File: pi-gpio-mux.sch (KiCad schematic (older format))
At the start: 31 parts, among them J1 Raspberry_Pi_2_3, J2 Raw, J3 Buffered, J4 Register-1, J5 Register-2, J6 Clk1, J7 Clk1, U1 74AHCT245, U10 74AHCT574, U11 74AHCT574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

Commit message: First layout template vias.
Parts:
- J7: value Clk1 -> Clk2
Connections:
- net CLK1: now reaches J6.1 (Pin_1), U5.11 (Cp), U6.11 (Cp), U7.11 (Cp), U8.11 (Cp)
- net CLK2: now reaches J7.1 (Pin_1), U10.11 (Cp), U11.11 (Cp), U12.11 (Cp), U9.11 (Cp)
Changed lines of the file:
@@
 P 9000 3900
 F 0 "J7" V 8964 3812 50  0000 R CNN
-F 1 "Clk1" V 8873 3812 50  0000 R CNN
+F 1 "Clk2" V 8873 3812 50  0000 R CNN
 F 2 "Connector_Pin:Pin_D0.7mm_L6.5mm_W1.8mm_FlatFork" H 9000 3900 50  0001 C CNN
 F 3 "~" H 9000 3900 50  0001 C CNN
@@
 	1    0    0    -1
 $EndComp
+Text Label 4850 4250 0    50   ~ 0
+CLK1
+Text Label 8900 4300 0    50   ~ 0
+CLK2
 $EndSCHEMATC

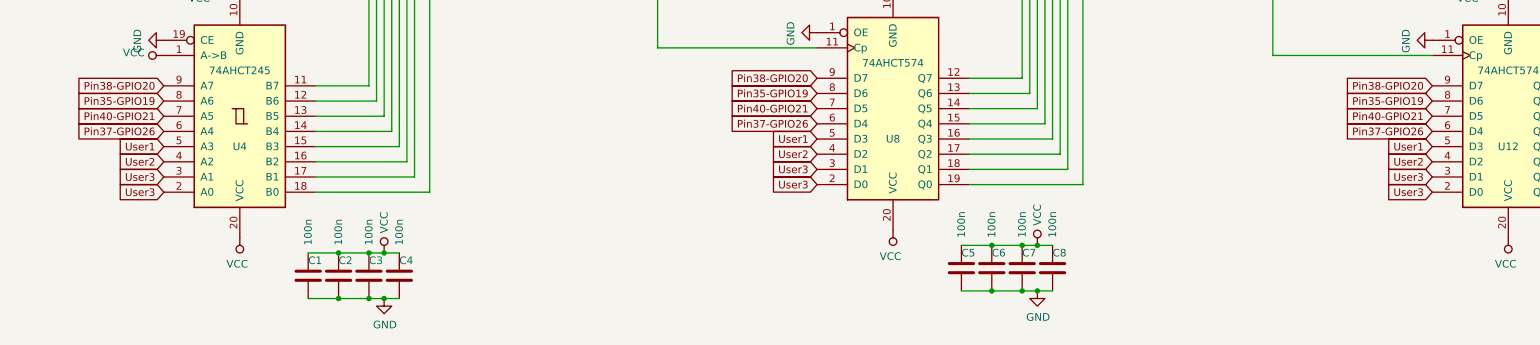
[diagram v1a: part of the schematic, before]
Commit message: trace signal between connectors.
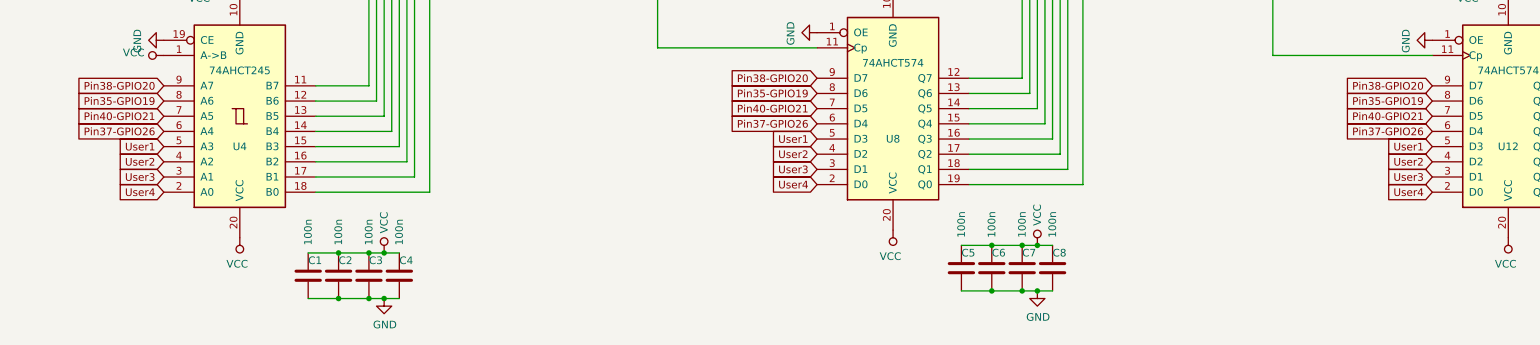
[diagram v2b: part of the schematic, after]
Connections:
- net User3: no longer U12.2 (D0), U4.2 (A0), U8.2 (D0)
- new net User4: U12.2 (D0), U4.2 (A0), U8.2 (D0)
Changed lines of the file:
@@
 User3
 Text GLabel 1600 10200 0    50   Input ~ 0
-User3
+User4
 $Comp
 L 74xx:74HCT574 U5
@@
 User3
 Text GLabel 5900 10150 0    50   Input ~ 0
-User3
+User4
 $Comp
 L 74xx:74HCT574 U6
@@
 User3
 Text GLabel 9950 10200 0    50   Input ~ 0
-User3
+User4
 $Comp
 L 74xx:74HCT574 U10

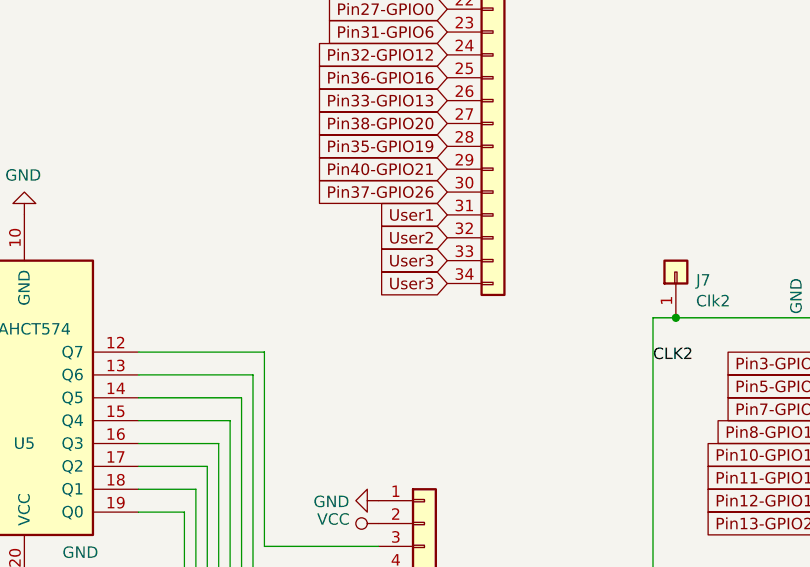
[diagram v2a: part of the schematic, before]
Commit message: Bus connect between registers.
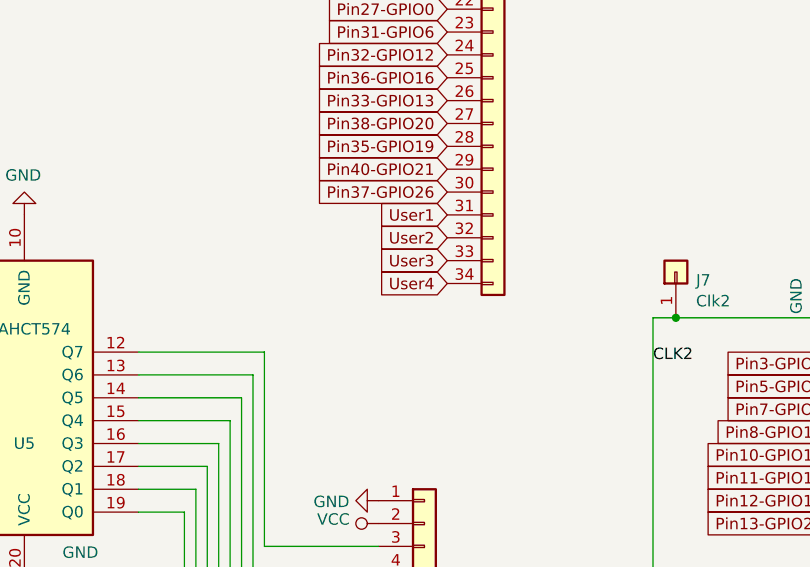
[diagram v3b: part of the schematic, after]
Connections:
- net User3: no longer J2.34 (Pin_34)
- net User4: now also J2.34 (Pin_34)
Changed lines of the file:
@@
 User3
 Text GLabel 8000 3950 0    50   Input ~ 0
-User3
+User4
 Text GLabel 1350 4300 0    50   Input ~ 0
 Pin3-GPIO2

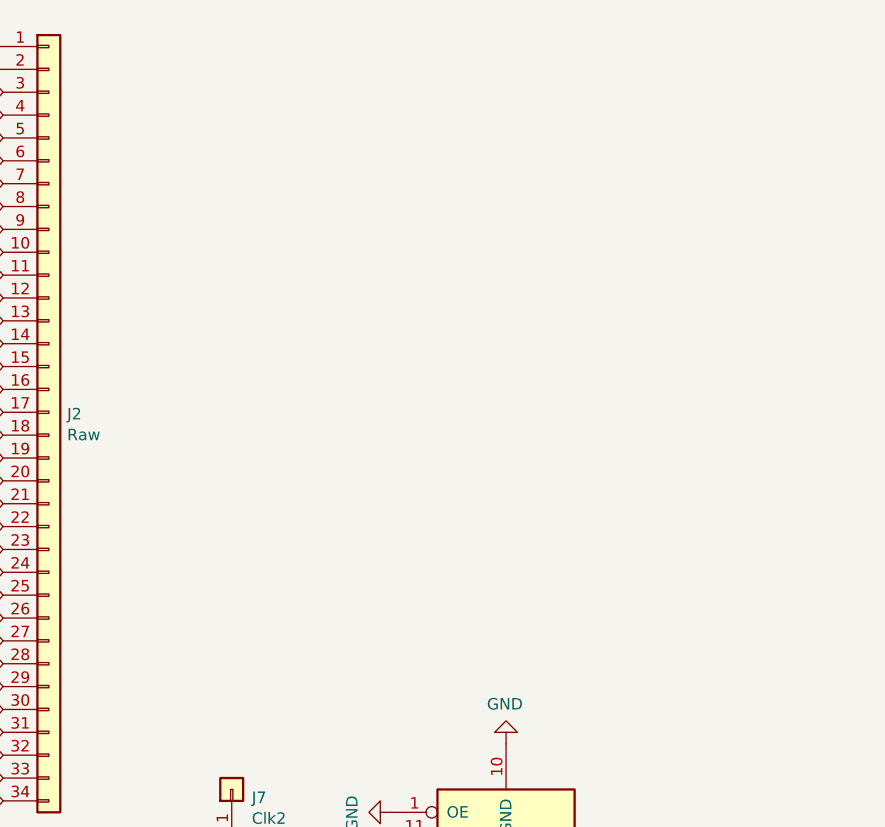
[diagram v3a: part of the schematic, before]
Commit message: Add inverters.
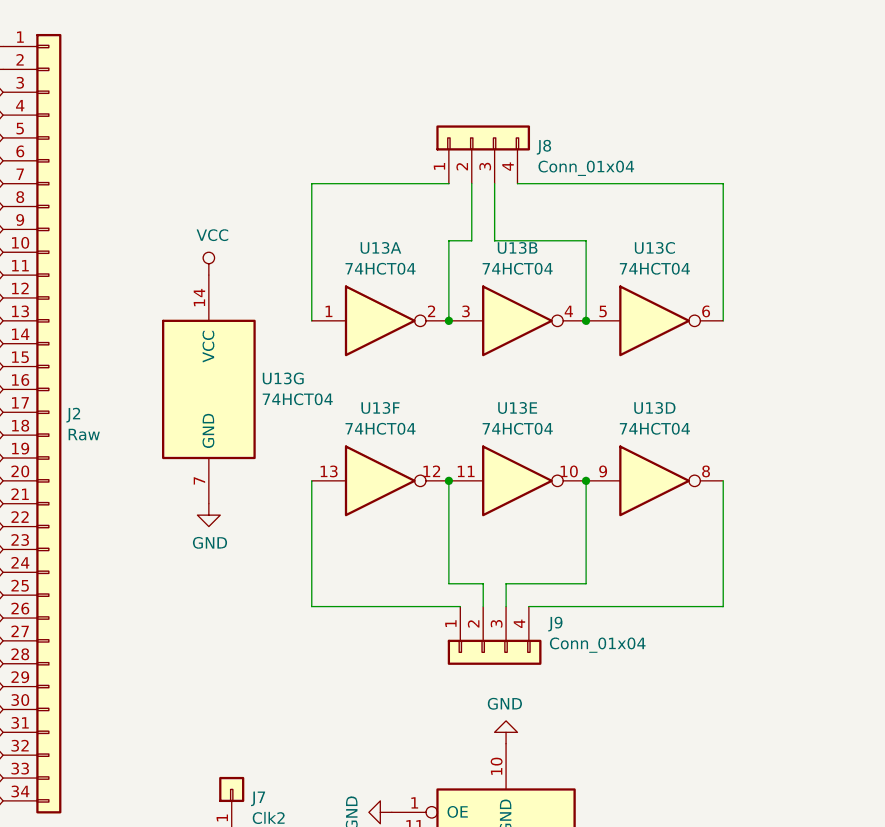
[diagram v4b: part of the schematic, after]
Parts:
- added J8, J9: Conn_01x04, pi-gpio-mux:triple-inverter, symbol Connector_Generic:Conn_01x04
- added U13: 74HCT04, pi-gpio-mux:SOT762-1-DHVQFN14, symbol 74xx:74HCT04
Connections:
- net GND: now also U13.7 (GND)
- net VCC: now also U13.14 (VCC)
- new net: J8.1 (Pin_1), U13.1
- new net: J8.2 (Pin_2), U13.2, U13.3
- new net: J8.3 (Pin_3), U13.4, U13.5
- new net: J8.4 (Pin_4), U13.6
- new net: J9.4 (Pin_4), U13.8
- new net: J9.3 (Pin_3), U13.10, U13.9
- new net: J9.2 (Pin_2), U13.11, U13.12
- new net: J9.1 (Pin_1), U13.13
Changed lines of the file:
@@
 Text Label 8900 4300 0    50   ~ 0
 CLK2
+$Comp
+L power:GND #PWR02
+U 1 1 5D3F4AF0
+P 8900 2650
+F 0 "#PWR02" H 8900 2400 50  0001 C CNN
+F 1 "GND" H 8905 2477 50  0000 C CNN
+F 2 "" H 8900 2650 50  0001 C CNN
+F 3 "" H 8900 2650 50  0001 C CNN
+	1    8900 2650
+	1    0    0    -1
+$EndComp
+$Comp
+L power:VCC #PWR01
+U 1 1 5D3F56BE
+P 8900 1650
+F 0 "#PWR01" H 8900 1500 50  0001 C CNN
+F 1 "VCC" H 8917 1823 50  0000 C CNN
+F 2 "" H 8900 1650 50  0001 C CNN
+F 3 "" H 8900 1650 50  0001 C CNN
+	1    8900 1650
+	1    0    0    -1
+$EndComp
+Wire Wire Line
+	10550 1500 10550 1850
+Wire Wire Line
+	9950 1500 9950 1850
+$Comp
+L 74xx:74HCT04 U13
+U 1 1 5D4B4710
+P 9650 1850
+F 0 "U13" H 9650 2167 50  0000 C CNN
+F 1 "74HCT04" H 9650 2076 50  0000 C CNN
+F 2 "pi-gpio-mux:SOT762-1-DHVQFN14" H 9650 1850 50  0001 C CNN
+F 3 "https://assets.nexperia.com/documents/data-sheet/74HC_HCT04.pdf" H 9650 1850 50  0001 C CNN
+	1    9650 1850
+	1    0    0    -1
+$EndComp
+$Comp
+L 74xx:74HCT04 U13
+U 2 1 5D4B5F00
+P 10250 1850
+F 0 "U13" H 10250 2167 50  0000 C CNN
+F 1 "74HCT04" H 10250 2076 50  0000 C CNN
+F 2 "pi-gpio-mux:SOT762-1-DHVQFN14" H 10250 1850 50  0001 C CNN
+F 3 "https://assets.nexperia.com/documents/data-sheet/74HC_HCT04.pdf" H 10250 1850 50  0001 C CNN
+	2    10250 1850
+	1    0    0    -1
+$EndComp
+Connection ~ 9950 1850
+$Comp
+L 74xx:74HCT04 U13
+U 3 1 5D4B7406
+P 10850 1850
+F 0 "U13" H 10850 2167 50  0000 C CNN
+F 1 "74HCT04" H 10850 2076 50  0000 C CNN
+F 2 "pi-gpio-mux:SOT762-1-DHVQFN14" H 10850 1850 50  0001 C CNN
+F 3 "https://assets.nexperia.com/documents/data-sheet/74HC_HCT04.pdf" H 10850 1850 50  0001 C CNN
+	3    10850 1850
+	1    0    0    -1
+$EndComp
+Connection ~ 10550 1850
+$Comp
+L 74xx:74HCT04 U13
+U 4 1 5D4B8FD4
+P 10850 2550
+F 0 "U13" H 10850 2867 50  0000 C CNN
+F 1 "74HCT04" H 10850 2776 50  0000 C CNN
+F 2 "pi-gpio-mux:SOT762-1-DHVQFN14" H 10850 2550 50  0001 C CNN
+F 3 "https://assets.nexperia.com/documents/data-sheet/74HC_HCT04.pdf" H 10850 2550 50  0001 C CNN
+	4    10850 2550
+	1    0    0    -1
+$EndComp
+$Comp
+L 74xx:74HCT04 U13
+U 5 1 5D4BAB75
+P 10250 2550
+F 0 "U13" H 10250 2867 50  0000 C CNN
+F 1 "74HCT04" H 10250 2776 50  0000 C CNN
+F 2 "pi-gpio-mux:SOT762-1-DHVQFN14" H 10250 2550 50  0001 C CNN
+F 3 "https://assets.nexperia.com/documents/data-sheet/74HC_HCT04.pdf" H 10250 2550 50  0001 C CNN
+	5    10250 2550
+	1    0    0    -1
+$EndComp
+Connection ~ 9950 2550
+$Comp
+L 74xx:74HCT04 U13
+U 6 1 5D4BC431
+P 9650 2550
+F 0 "U13" H 9650 2867 50  0000 C CNN
+F 1 "74HCT04" H 9650 2776 50  0000 C CNN
+F 2 "pi-gpio-mux:SOT762-1-DHVQFN14" H 9650 2550 50  0001 C CNN
+F 3 "https://assets.nexperia.com/documents/data-sheet/74HC_HCT04.pdf" H 9650 2550 50  0001 C CNN
+	6    9650 2550
+	1    0    0    -1
+$EndComp
+Connection ~ 10550 2550
+$Comp
+L 74xx:74HCT04 U13
+U 7 1 5D4BE165
+P 8900 2150
+F 0 "U13" H 9130 2196 50  0000 L CNN
+F 1 "74HCT04" H 9130 2105 50  0000 L CNN
+F 2 "pi-gpio-mux:SOT762-1-DHVQFN14" H 8900 2150 50  0001 C CNN
+F 3 "https://assets.nexperia.com/documents/data-sheet/74HC_HCT04.pdf" H 8900 2150 50  0001 C CNN
+	7    8900 2150
+	1    0    0    -1
+$EndComp
+$Comp
+L Connector_Generic:Conn_01x04 J8
+U 1 1 5D4D6C84
+P 10050 1050
+F 0 "J8" V 10014 762 50  0000 R CNN
+F 1 "Conn_01x04" V 9923 762 50  0000 R CNN
+F 2 "pi-gpio-mux:triple-inverter" H 10050 1050 50  0001 C CNN
+F 3 "~" H 10050 1050 50  0001 C CNN
+	1    10050 1050
+	0    -1   -1   0
+$EndComp
+Wire Wire Line
+	9950 1250 9350 1250
+Wire Wire Line
+	9350 1250 9350 1850
+Wire Wire Line
+	10050 1250 10050 1500
+Wire Wire Line
+	10050 1500 9950 1500
+Wire Wire Line
+	10150 1250 10150 1500
+Wire Wire Line
+	10150 1500 10550 1500
+Wire Wire Line
+	10250 1250 11150 1250
+Wire Wire Line
+	11150 1250 11150 1850
+$Comp
+L Connector_Generic:Conn_01x04 J9
+U 1 1 5D54A0CE
+P 10100 3300
+F 0 "J9" V 9972 3012 50  0000 R CNN
+F 1 "Conn_01x04" V 10063 3012 50  0000 R CNN
+F 2 "pi-gpio-mux:triple-inverter" H 10100 3300 50  0001 C CNN
+F 3 "~" H 10100 3300 50  0001 C CNN
+	1    10100 3300
+	0    -1   1    0
+$EndComp
+Wire Wire Line
+	9350 3100 10000 3100
+Wire Wire Line
+	9350 2550 9350 3100
+Wire Wire Line
+	10300 3100 11150 3100
+Wire Wire Line
+	11150 2550 11150 3100
+Wire Wire Line
+	10550 3000 10200 3000
+Wire Wire Line
+	10200 3000 10200 3100
+Wire Wire Line
+	10550 2550 10550 3000
+Wire Wire Line
+	9950 3000 10100 3000
+Wire Wire Line
+	10100 3000 10100 3100
+Wire Wire Line
+	9950 2550 9950 3000
 $EndSCHEMATC
